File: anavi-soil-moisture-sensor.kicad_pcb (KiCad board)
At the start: 2 copper layers, 22.9 x 61 mm, 9 parts, among them P1 CONN_01X03, P2 CONN_01X01, P3 CONN_01X01, Q1 BC817

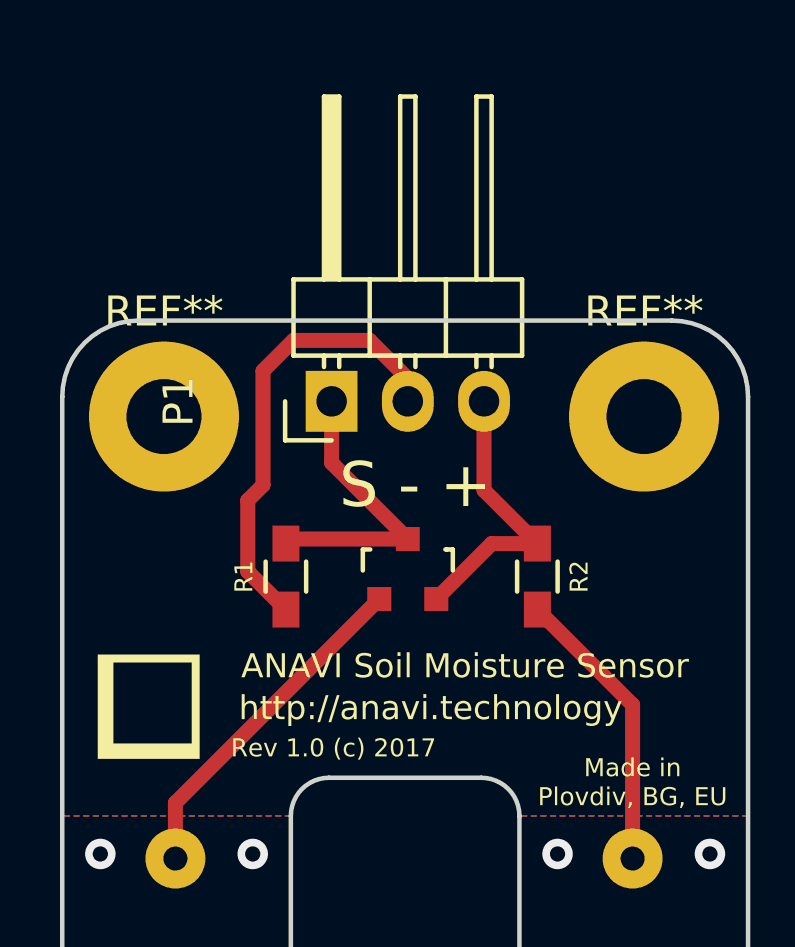
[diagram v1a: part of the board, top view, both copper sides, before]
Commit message: anavi-soil-moisture-sensor.kicad_pcb: update zones
Signed-off-by: Leon Anavi <leon@anavi.org>
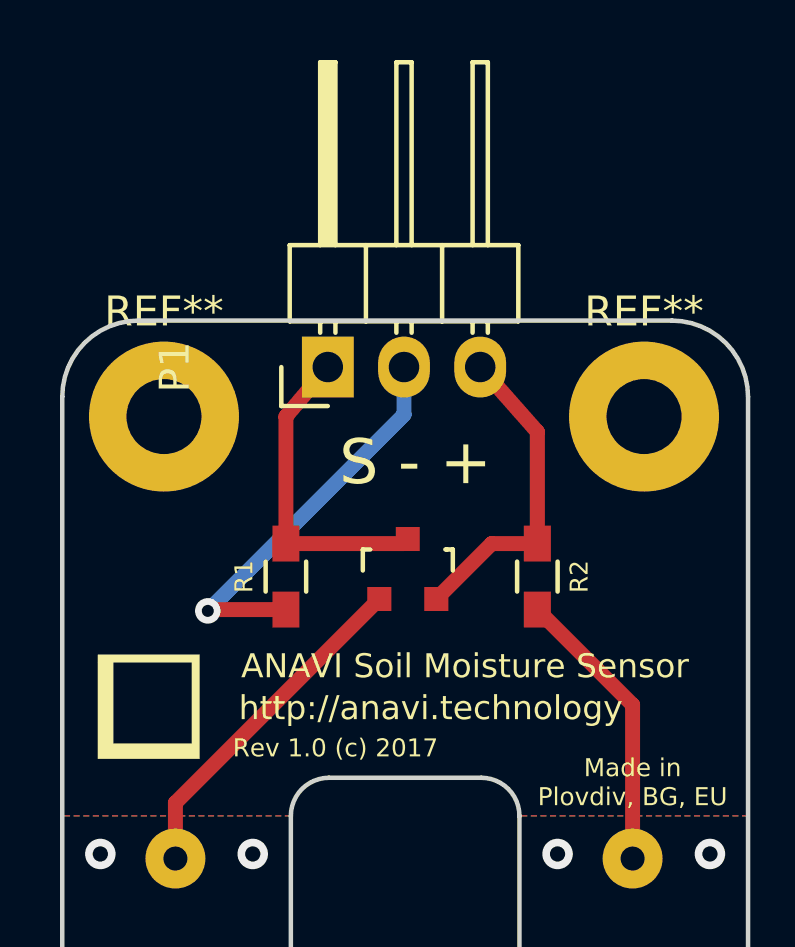
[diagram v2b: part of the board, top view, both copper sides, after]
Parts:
- moved P1 1.15 mm to (145.9, 76.1)
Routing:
- net +3V3: track 9.61 -> 10.7 mm
- net GND: track 15.2 -> 14.2 mm, vias 0 -> 1
- net Net-(P1-Pad1): track 9.77 -> 10.7 mm
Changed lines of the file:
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@@
     (links 7)
     (no_connects 0)
-    (area 136.996099 74.448599 160.006101 135.558601)
+    (area 130.493714 65.143999 166.432286 136.715501)
     (thickness 1.6)
     (drawings 45)
-    (tracks 60)
+    (tracks 59)
     (zones 0)
     (modules 9)
@@
   )
   (module Pin_Headers:Pin_Header_Angled_1x03 (layer Top)
-    (at 146.05 77.216 90)
+    (at 145.923 76.073 90)
     (descr "Through hole pin header")
     (tags "pin header")
@@
     (effects (font (size 0.6 0.6) (thickness 0.15)))
   )
-  (gr_text "Rev 1.0 (c) 2017" (at 146.1135 88.773) (layer F.SilkS)
+  (gr_text "Rev 1.0 (c) 2017" (at 146.177 88.773) (layer F.SilkS)
     (effects (font (size 0.6 0.6) (thickness 0.15)))
   )
@@
     (effects (font (size 0.8 0.8) (thickness 0.2)))
   )
-  (gr_text "S - +" (at 148.844 80.01) (layer F.SilkS)
+  (gr_text "S - +" (at 148.844 79.248) (layer F.SilkS)
     (effects (font (size 1.5 1.5) (thickness 0.3)))
   )
@@
   (gr_line (start 159.9311 127.8636) (end 159.9311 91.0336) (layer B.Mask) (width 0.15))
   (gr_line (start 159.9311 91.0336) (end 152.3111 91.0336) (layer B.Mask) (width 0.15))
+  (via (at 142.1511 97.3836) (size 1.016) (drill 0.508) (layers Top Bottom) (net 0))
+  (via (at 139.6111 97.3836) (size 1.016) (drill 0.508) (layers Top Bottom) (net 0))
+  (via (at 143.4211 92.3036) (size 1.016) (drill 0.508) (layers Top Bottom) (net 0))
   (via (at 153.5811 92.3036) (size 1.016) (drill 0.508) (layers Top Bottom) (net 0))
   (via (at 158.6611 92.3036) (size 1.016) (drill 0.508) (layers Top Bottom) (net 0))
@@
   (via (at 154.8511 117.7036) (size 1.016) (drill 0.508) (layers Top Bottom) (net 0))
   (via (at 157.3911 117.7036) (size 1.016) (drill 0.508) (layers Top Bottom) (net 0))
-  (via (at 143.4211 92.3036) (size 1.016) (drill 0.508) (layers Top Bottom) (net 0))
   (via (at 138.3411 92.3036) (size 1.016) (drill 0.508) (layers Top Bottom) (net 0))
   (via (at 138.3411 102.4636) (size 1.016) (drill 0.508) (layers Top Bottom) (net 0))
@@
   (via (at 139.6111 107.5436) (size 1.016) (drill 0.508) (layers Top Bottom) (net 0))
   (via (at 142.1511 107.5436) (size 1.016) (drill 0.508) (layers Top Bottom) (net 0))
-  (via (at 139.6111 97.3836) (size 1.016) (drill 0.508) (layers Top Bottom) (net 0))
-  (via (at 142.1511 97.3836) (size 1.016) (drill 0.508) (layers Top Bottom) (net 0))
-  (segment (start 148.59 77.216) (end 148.59 76.454) (width 0.5) (layer Top) (net 1))
-  (segment (start 148.59 76.454) (end 147.32 75.184) (width 0.5) (layer Top) (net 1))
-  (segment (start 147.32 75.184) (end 144.78 75.184) (width 0.5) (layer Top) (net 1))
-  (segment (start 144.78 75.184) (end 143.764 76.2) (width 0.5) (layer Top) (net 1))
-  (segment (start 143.764 76.2) (end 143.764 80.01) (width 0.5) (layer Top) (net 1))
-  (segment (start 143.764 80.01) (end 143.256 80.518) (width 0.5) (layer Top) (net 1))
-  (segment (start 143.256 80.518) (end 143.256 82.888) (width 0.5) (layer Top) (net 1))
-  (segment (start 143.256 82.888) (end 144.526 84.158) (width 0.5) (layer Top) (net 1))
-  (segment (start 148.59 81.80578) (end 144.67822 81.80578) (width 0.5) (layer Top) (net 4))
+  (segment (start 144.526 84.158) (end 141.9655 84.158) (width 0.5) (layer Top) (net 1))
+  (segment (start 148.463 77.6605) (end 148.463 76.073) (width 0.5) (layer Bottom) (net 1) (status 20))
+  (segment (start 141.9225 84.201) (end 148.463 77.6605) (width 0.5) (layer Bottom) (net 1))
+  (via (at 141.9225 84.201) (size 0.85) (drill 0.4) (layers Top Bottom) (net 1))
+  (segment (start 141.9655 84.158) (end 141.9225 84.201) (width 0.5) (layer Top) (net 1))
+  (segment (start 148.463 76.073) (end 148.463 75.311) (width 0.5) (layer Top) (net 1) (status 30))
+  (segment (start 144.526 81.958) (end 144.526 77.724) (width 0.5) (layer Top) (net 4))
+  (segment (start 144.526 77.724) (end 145.923 76.073) (width 0.5) (layer Top) (net 4) (status 20))
+  (segment (start 144.526 81.958) (end 148.43778 81.958) (width 0.5) (layer Top) (net 4))
+  (segment (start 148.43778 81.958) (end 148.59 81.80578) (width 0.5) (layer Top) (net 4))
   (segment (start 144.67822 81.80578) (end 144.526 81.958) (width 0.5) (layer Top) (net 4))
-  (segment (start 146.05 77.216) (end 146.05 79.26578) (width 0.5) (layer Top) (net 4))
-  (segment (start 146.05 79.26578) (end 148.59 81.80578) (width 0.5) (layer Top) (net 4))
+  (segment (start 152.908 81.958) (end 152.908 78.232) (width 0.5) (layer Top) (net 5))
+  (segment (start 152.908 78.232) (end 151.003 76.073) (width 0.5) (layer Top) (net 5) (status 20))
   (segment (start 152.908 81.958) (end 151.38676 81.958) (width 0.5) (layer Top) (net 5))
   (segment (start 151.38676 81.958) (end 149.54 83.80476) (width 0.5) (layer Top) (net 5))
-  (segment (start 151.13 77.216) (end 151.13 80.18) (width 0.5) (layer Top) (net 5))
-  (segment (start 151.13 80.18) (end 152.908 81.958) (width 0.5) (layer Top) (net 5))
   (segment (start 140.843 92.456) (end 140.843 90.60176) (width 0.5) (layer Top) (net 6))
   (segment (start 140.843 90.60176) (end 147.64 83.80476) (width 0.5) (layer Top) (net 6))
   (segment (start 156.083 92.456) (end 156.083 87.333) (width 0.5) (layer Top) (net 7))
   (segment (start 156.083 87.333) (end 152.908 84.158) (width 0.5) (layer Top) (net 7))
-  (zone (net 2) (net_name PROBE1) (layer Top) (hatch none 0.508)
+  (zone (net 3) (net_name PROBE2) (layer Top) (hatch none 0.508)
     (priority 6)
     (connect_pads (clearance 0.508))
@@
     (polygon
       (pts
-        (xy 152.3111 91.0336) (xy 152.3111 135.4836) (xy 159.9311 135.4836) (xy 159.9311 91.0336)
+        (xy 137.0711 91.0336) (xy 137.0711 135.4836) (xy 144.6911 135.4836) (xy 144.6911 91.0336)
+      )
+    )
+  )
+  (zone (net 3) (net_name PROBE2) (layer Bottom) (hatch none 0.508)
+    (priority 6)
+    (connect_pads (clearance 0.508))
+    (min_thickness 0.254)
+    (fill yes (arc_segments 32) (thermal_gap 0.304) (thermal_bridge_width 0.304))
+    (polygon
+      (pts
+        (xy 137.0711 91.0336) (xy 137.0711 135.4836) (xy 144.6911 135.4836) (xy 144.6911 91.0336)
       )
     )
@@
     )
   )
-  (zone (net 3) (net_name PROBE2) (layer Top) (hatch none 0.508)
+  (zone (net 2) (net_name PROBE1) (layer Top) (hatch none 0.508)
     (priority 6)
     (connect_pads (clearance 0.508))
@@
     (polygon
       (pts
-        (xy 137.0711 91.0336) (xy 137.0711 135.4836) (xy 144.6911 135.4836) (xy 144.6911 91.0336)
-      )
-    )
-  )
-  (zone (net 3) (net_name PROBE2) (layer Bottom) (hatch none 0.508)
-    (priority 6)
-    (connect_pads (clearance 0.508))
-    (min_thickness 0.254)
-    (fill yes (arc_segments 32) (thermal_gap 0.304) (thermal_bridge_width 0.304))
-    (polygon
-      (pts
-        (xy 137.0711 91.0336) (xy 137.0711 135.4836) (xy 144.6911 135.4836) (xy 144.6911 91.0336)
+        (xy 152.3111 91.0336) (xy 152.3111 135.4836) (xy 159.9311 135.4836) (xy 159.9311 91.0336)
       )
     )
@@
     (polygon
       (pts
-        (xy 162.306 138.938) (xy 135.382 138.938) (xy 135.255 91.059) (xy 162.306 91.059)
+        (xy 145.2245 136.5885) (xy 136.398 136.652) (xy 136.398 91.059) (xy 145.288 91.059)
       )
     )
@@
     (polygon
       (pts
-        (xy 162.306 138.938) (xy 135.382 138.938) (xy 135.255 91.059) (xy 162.306 91.059)
-      )
-    )
+        (xy 145.2245 136.5885) (xy 136.398 136.652) (xy 136.398 91.059) (xy 145.288 91.059)
+      )
+    )
+  )
+  (zone (net 0) (net_name "") (layer F.Mask) (hatch edge 0.508)
+    (connect_pads (clearance 0.508))
+    (min_thickness 0.254)
+    (fill yes (arc_segments 16) (thermal_gap 0.508) (thermal_bridge_width 0.508))
+    (polygon
+      (pts
+        (xy 160.5915 136.652) (xy 151.7015 136.7155) (xy 151.765 91.059) (xy 160.4645 91.059)
+      )
+    )
+  )
+  (zone (net 0) (net_name "") (layer B.Mask) (hatch edge 0.508)
+    (connect_pads (clearance 0.508))
+    (min_thickness 0.254)
+    (fill yes (arc_segments 16) (thermal_gap 0.508) (thermal_bridge_width 0.508))
+    (polygon
+      (pts
+        (xy 160.5915 136.652) (xy 151.7015 136.7155) (xy 151.765 91.059) (xy 160.4645 91.059)
+      )
+    )
